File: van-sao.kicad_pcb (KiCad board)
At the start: 2 copper layers, 57 x 43 mm, 6 parts, among them X1 Badgelife_shitty_connector

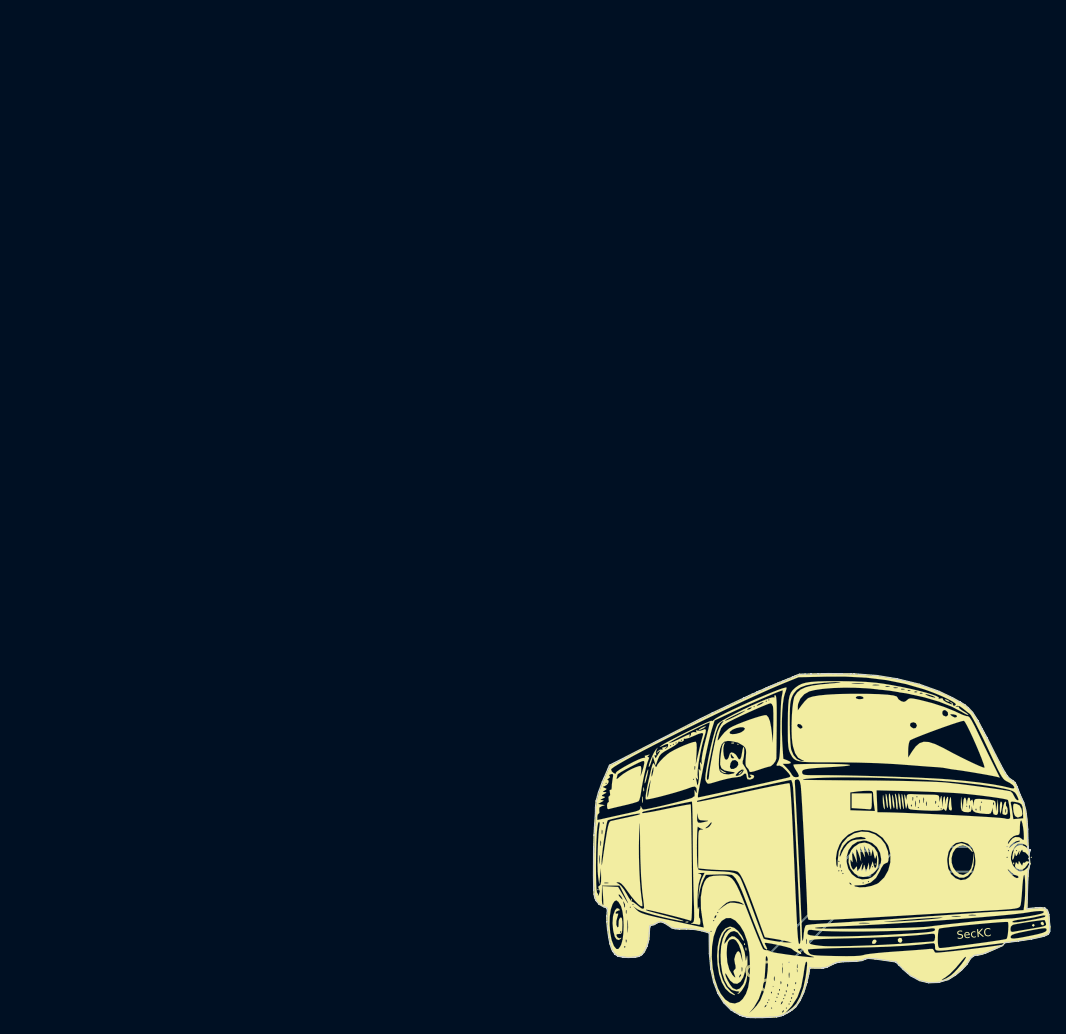
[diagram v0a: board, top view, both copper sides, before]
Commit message: getting svg2shenzen artwork implemented
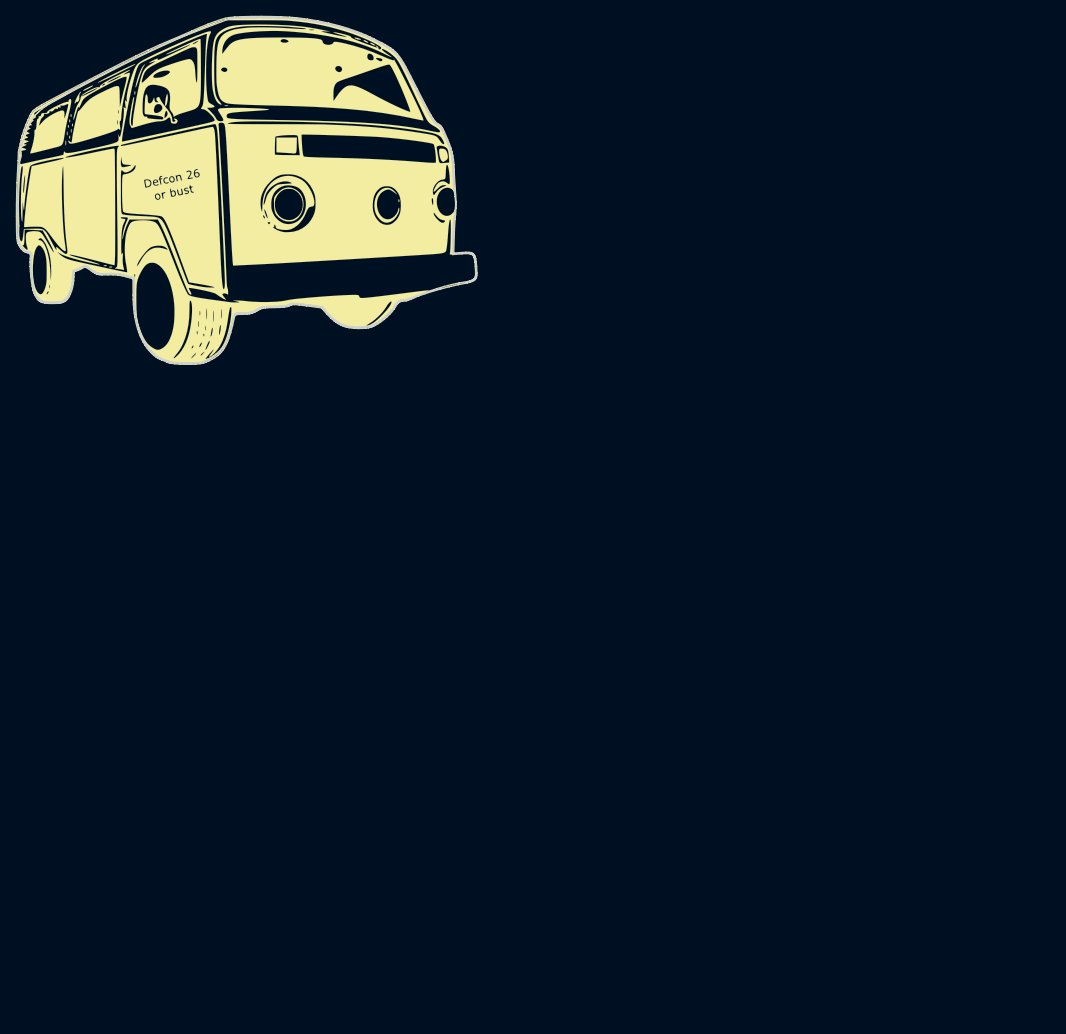
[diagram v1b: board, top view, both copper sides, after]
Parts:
- removed D1, D2: LED, LED_SMD:LED_1206_3216Metric_ReverseMount_Hole1.8x2.4mm
- removed the G*** at (52.6, 86.4)
- removed the G*** at (71.9, 81.9)
- removed R1: 1K, Resistor_SMD:R_1206_3216Metric
- removed X1: Badgelife_shitty_connector, my-ki-cad-parts:Badgelife-Shitty-2x2
- added G*** (x3): LOGO, LOGO, F.Cu at (0.00, 0.00)
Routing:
- net Net-(D1-Pad1): track 20.7 -> 0.00 mm
- net Net-(D1-Pad2): track 19.7 -> 0.00 mm
- net Net-(D2-Pad1): track 19.2 -> 0.00 mm
- net Net-(R1-Pad2): track 12.5 -> 0.00 mm
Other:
- board size 57 x 43 mm -> 57.6 x 43.5 mm
- net class Default: via_dia 0.8 -> 0.6
- rule pad_to_mask_clearance: 0.051 -> 0.2
- board text removed: "SecKC"
- board text removed: "SecKC Road Crew Defcon 26"
- board text removed: "sysarron DeadTr33"

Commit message: updated gerbers for new art
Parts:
- removed the G*** at (0.00, 0.00) (x3)
- added G*** (x3): LOGO, LOGO, F.Cu at (0.00, 0.00)
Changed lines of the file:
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@@
     (visible_elements 7FFFFFFF)
     (pcbplotparams
-      (layerselection 0x010f0_80000001)
+      (layerselection 0x010f0_ffffffff)
       (usegerberextensions false)
       (usegerberattributes false)
@@
       (outputformat 1)
       (mirror false)
-      (drillshape 1)
+      (drillshape 0)
       (scaleselection 1)
       (outputdirectory "gerbers/"))

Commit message: final for first production run
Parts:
- removed the G*** at (0.00, 0.00) (x3)
- added D1: LED, LED_SMD:LED_1206_3216Metric, B.Cu at (22.1, 1.58)
- added D2: LED, LED_SMD:LED_1206_3216Metric, B.Cu at (2.09, 1.95)
- added G*** (x3): LOGO, LOGO, F.Cu at (0.00, 0.00)
- added G***: LOGO, LOGO, F.Cu at (-0.03, -0.03)
- added R1: 1K, Resistor_SMD:R_0805_2012Metric, B.Cu at (-9.71, 3.17)
- added X1: Badgelife_shitty_connector, my-ki-cad-parts:Badgelife-Shitty-2x2, B.Cu at (-22.0, 5.23)
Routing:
- net Net-(D1-Pad2): track 0.00 -> 35.5 mm
- net Net-(D2-Pad1): track 0.00 -> 25.9 mm
- net Net-(R1-Pad2): track 0.00 -> 25.2 mm
- net Net-(D1-Pad1): track 0.00 -> 22.8 mm
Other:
- outline, holes or cut-outs redrawn
- board text added: "DeadTr33"
- board text added: "SecKC Defcon26 Road Crew:"
- board text added: "sysaaron"
